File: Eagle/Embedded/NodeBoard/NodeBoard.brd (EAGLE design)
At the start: 121.7 x 96 mm, 68 parts, among them IC1 7812TV, IC2 5v, IC3 3v3, IC4 REG1117, IC5 REG1117, J1 DCJ0202, Q2 IRF740, T1 BC547

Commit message: Minor Eagle Board fixes
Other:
- board size 121.7 x 96 mm -> 121.3 x 95.8 mm

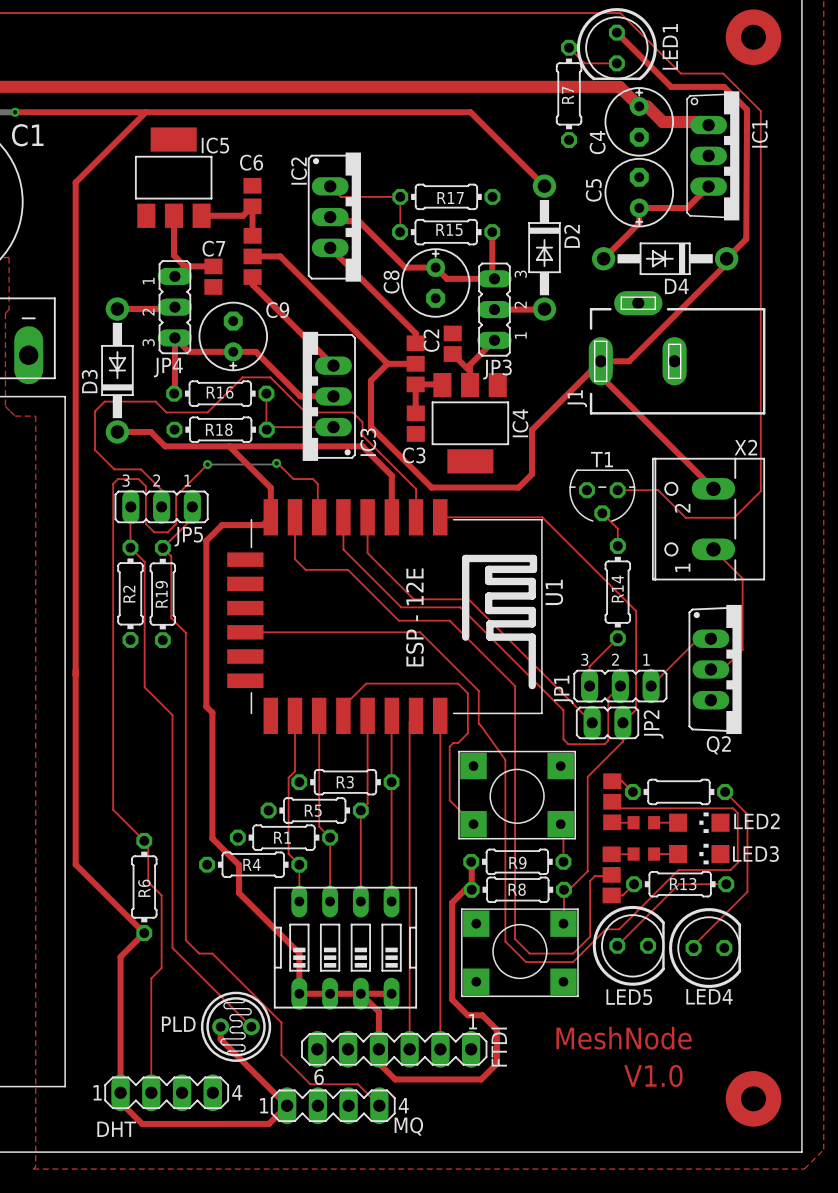
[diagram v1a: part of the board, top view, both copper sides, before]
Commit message: Eagle Flipped directional components
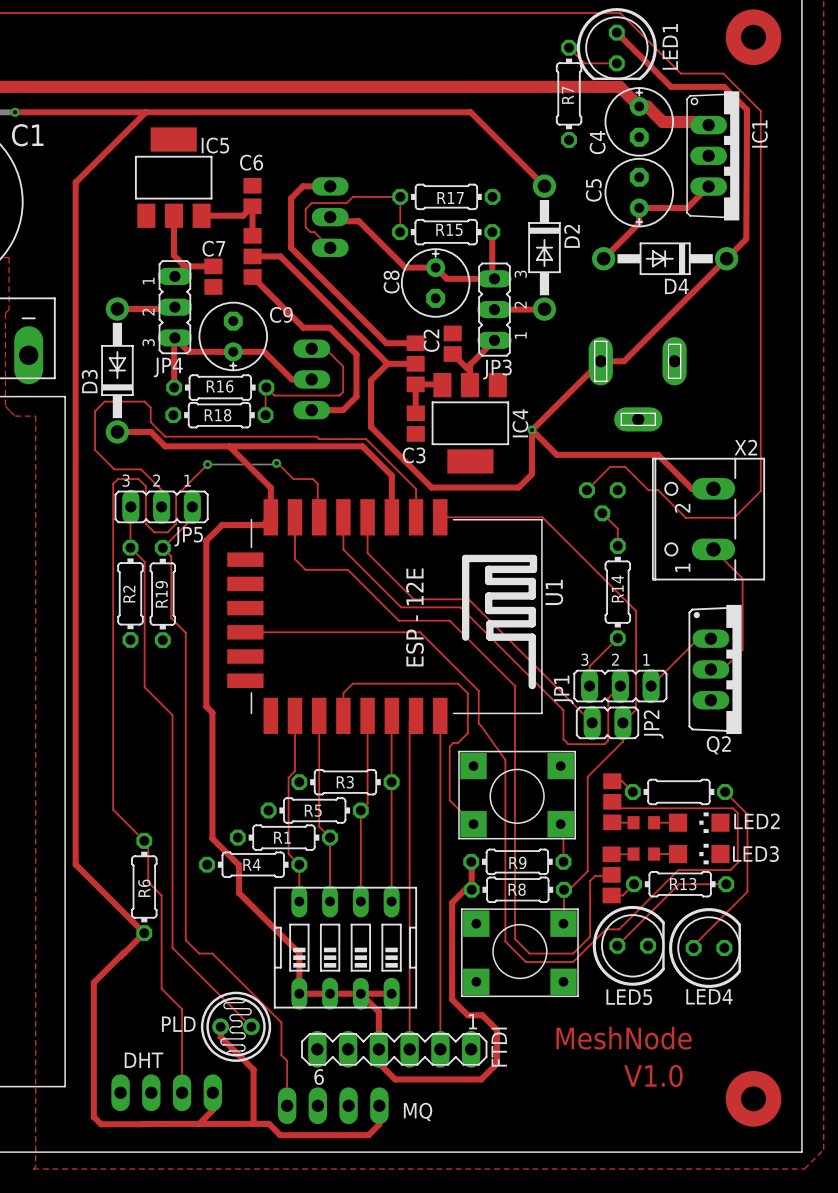
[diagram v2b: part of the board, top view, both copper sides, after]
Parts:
- moved IC3 2.28 mm to (-48.3, 147.6), flipped to the bottom, turned to 270 degrees
- moved R18 1.20 mm to (-53.4, 144.7)
- moved R16 0.50 mm to (-53.4, 147.0)
- flipped DHT to the bottom
- flipped IC2 to the bottom, turned to 90 degrees
- flipped J1 to the bottom, turned to 270 degrees
- flipped MQ to the bottom
- flipped T1 to the bottom
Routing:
- net VCC: track 199.3 -> 215.9 mm
- net N$49: track 10.8 -> 21.3 mm
- net N$50: track 10.1 -> 18.9 mm
- net N$46: track 9.07 -> 15.4 mm
- net N$48: track 8.59 -> 14.4 mm
- net N$9: track 60.8 -> 55.4 mm
- net N$42: track 154.3 -> 158.4 mm
- net N$47: track 19.7 -> 17.3 mm
- net 12V: track 105.4 -> 107.7 mm, vias 0 -> 1
- net N$3: track 46.7 -> 44.4 mm
- net N$22: track 24.7 -> 26.1 mm

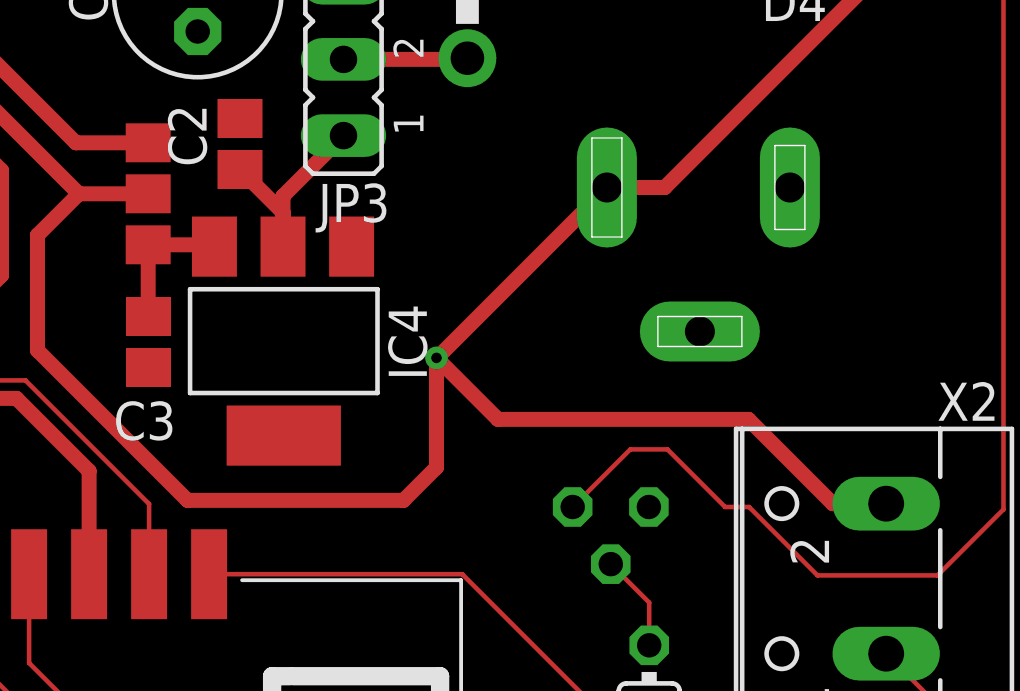
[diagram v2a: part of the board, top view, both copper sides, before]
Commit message: Eagle via fix
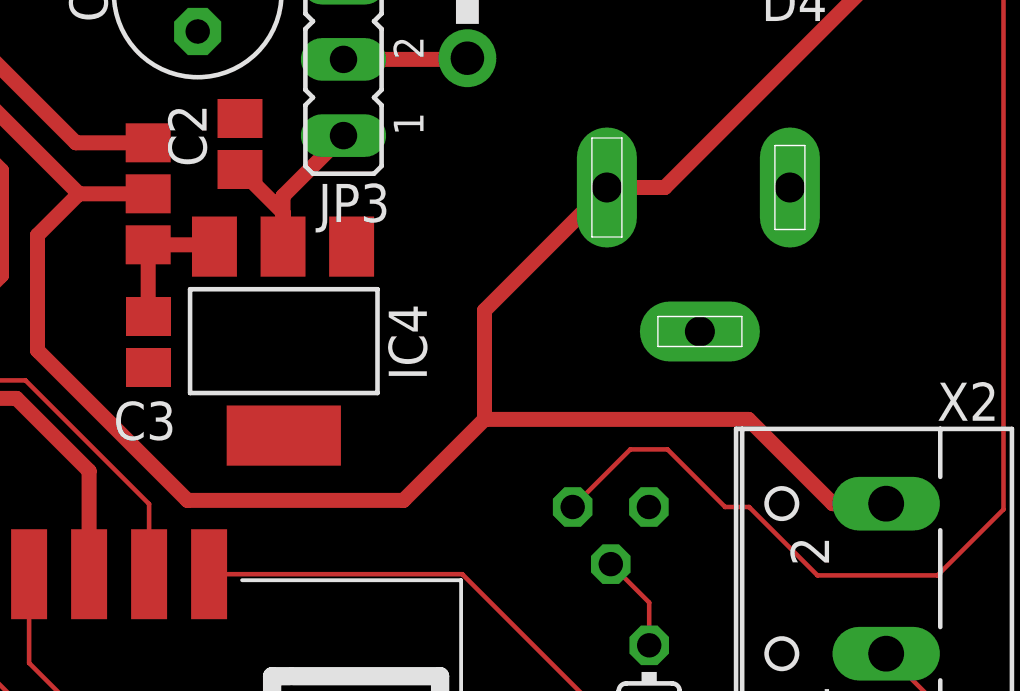
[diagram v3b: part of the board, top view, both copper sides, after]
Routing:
- net 12V: track 107.7 -> 105.3 mm, vias 1 -> 0
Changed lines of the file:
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@@
 <layer number="45" name="Holes" color="7" fill="1" visible="yes" active="yes"/>
 <layer number="46" name="Milling" color="3" fill="1" visible="yes" active="yes"/>
-<layer number="47" name="Measures" color="7" fill="1" visible="yes" active="yes"/>
-<layer number="48" name="Document" color="7" fill="1" visible="yes" active="yes"/>
-<layer number="49" name="Reference" color="7" fill="1" visible="yes" active="yes"/>
+<layer number="47" name="Measures" color="7" fill="1" visible="no" active="yes"/>
+<layer number="48" name="Document" color="7" fill="1" visible="no" active="yes"/>
+<layer number="49" name="Reference" color="7" fill="1" visible="no" active="yes"/>
 <layer number="50" name="dxf" color="7" fill="1" visible="no" active="no"/>
 <layer number="51" name="tDocu" color="7" fill="1" visible="yes" active="yes"/>
@@
 <wire x1="-48.39" y1="157.79" x2="-50.68" y2="157.79" width="0.5" layer="1"/>
 <wire x1="-39.52" y1="148.92" x2="-48.39" y2="157.79" width="0.5" layer="1"/>
-<wire x1="-27.6" y1="139.8" x2="-27.6" y2="143.45" width="0.5" layer="1"/>
-<wire x1="-27.6" y1="139.8" x2="-28.7" y2="138.7" width="0.5" layer="1"/>
 <wire x1="-35.9" y1="138.7" x2="-40.9" y2="143.7" width="0.5" layer="1"/>
 <wire x1="-40.9" y1="143.7" x2="-40.9" y2="147.54" width="0.5" layer="1"/>
 <wire x1="-40.9" y1="147.54" x2="-39.52" y2="148.92" width="0.5" layer="1"/>
-<wire x1="-28.7" y1="138.7" x2="-35.9" y2="138.7" width="0.5" layer="1"/>
-<via x="-27.6" y="143.45" extent="1-16" drill="0.35"/>
+<wire x1="-35.9" y1="138.7" x2="-28.7" y2="138.7" width="0.5" layer="1"/>
 <wire x1="-11.52" y1="157.6" x2="-19.99" y2="149.13" width="0.5" layer="1"/>
 <wire x1="-12.61" y1="138.59" x2="-14.39" y2="138.59" width="0.5" layer="1"/>
-<wire x1="-14.39" y1="138.59" x2="-17.2" y2="141.4" width="0.5" layer="1"/>
-<wire x1="-17.2" y1="141.4" x2="-25.55" y2="141.4" width="0.5" layer="1"/>
-<wire x1="-25.55" y1="141.4" x2="-27.6" y2="143.45" width="0.5" layer="1"/>
+<wire x1="-17.2" y1="141.4" x2="-14.39" y2="138.59" width="0.5" layer="1"/>
 <wire x1="-21.9" y1="149.13" x2="-19.99" y2="149.13" width="0.5" layer="1"/>
 <wire x1="-21.9" y1="149.13" x2="-21.92" y2="149.13" width="0.5" layer="1"/>
-<wire x1="-27.6" y1="143.45" x2="-27.58" y2="143.45" width="0.5" layer="1"/>
-<wire x1="-27.58" y1="143.45" x2="-21.9" y2="149.13" width="0.5" layer="1"/>
+<wire x1="-28.7" y1="138.7" x2="-26" y2="141.4" width="0.5" layer="1"/>
+<wire x1="-26" y1="141.4" x2="-17.2" y2="141.4" width="0.5" layer="1"/>
+<wire x1="-26" y1="141.4" x2="-26" y2="145.03" width="0.5" layer="1"/>
+<wire x1="-26" y1="145.03" x2="-21.9" y2="149.13" width="0.5" layer="1"/>
 </signal>
 <signal name="N$21">

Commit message: Fix dimentions
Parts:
- moved J1 3.01 mm to (-15.8, 149.3)
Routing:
- net 12V: track 105.3 -> 104.1 mm
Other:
- board size 121.3 x 95.8 mm -> 121.1 x 96 mm
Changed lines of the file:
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@@
 <board>
 <plain>
-<wire x1="-126.6" y1="179.6" x2="-126.6" y2="83.8" width="0" layer="20"/>
-<wire x1="-126.6" y1="83.8" x2="-5.3" y2="83.8" width="0" layer="20"/>
-<wire x1="-5.3" y1="83.8" x2="-5.3" y2="179.6" width="0" layer="20"/>
-<wire x1="-5.3" y1="179.6" x2="-126.6" y2="179.6" width="0" layer="20"/>
+<wire x1="-126.4" y1="179.7" x2="-126.3" y2="83.7" width="0" layer="20"/>
+<wire x1="-126.3" y1="83.7" x2="-5.3" y2="83.7" width="0" layer="20"/>
+<wire x1="-5.3" y1="83.7" x2="-5.3" y2="179.7" width="0" layer="20"/>
+<wire x1="-5.3" y1="179.7" x2="-126.4" y2="179.7" width="0" layer="20"/>
 <circle x="-120.5" y="89.7" radius="1.66433125" width="1.27" layer="1"/>
 <circle x="-121.4" y="176" radius="1.66433125" width="1.27" layer="1"/>
@@
 <text x="-25.8" y="92.3" size="1.778" layer="1">MeshNode</text>
 <text x="-20" y="89.2" size="1.778" layer="1">V1.0</text>
+<dimension x1="-126.3" y1="179.6" x2="-5.3" y2="179.6" x3="-65.8" y3="183.3" textsize="1.778" layer="1"/>
+<dimension x1="-126.3" y1="179.7" x2="-126.3" y2="83.7" x3="-127.8" y3="131.7" textsize="1.778" layer="1"/>
 </plain>
 <attributes>
@@
 <attribute name="OC_NEWARK" value="14P6981" x="-57.2" y="164.3" size="1.778" layer="27" display="off"/>
 </element>
-<element name="J1" library="con-jack" package="DCJ0202" value="DCJ0202" x="-18.82" y="149.13" smashed="yes" rot="MR270">
-<attribute name="MF" value="" x="-18.82" y="149.13" size="1.778" layer="28" rot="MR270" display="off"/>
-<attribute name="MPN" value="" x="-18.82" y="149.13" size="1.778" layer="28" rot="MR270" display="off"/>
-<attribute name="NAME" x="-23.4" y="152.84" size="1.27" layer="26" rot="MR270"/>
-<attribute name="OC_FARNELL" value="unknown" x="-18.82" y="149.13" size="1.778" layer="28" rot="MR270" display="off"/>
-<attribute name="OC_NEWARK" value="unknown" x="-18.82" y="149.13" size="1.778" layer="28" rot="MR270" display="off"/>
+<element name="J1" library="con-jack" package="DCJ0202" value="DCJ0202" x="-15.82" y="149.33" smashed="yes" rot="MR270">
+<attribute name="MF" value="" x="-15.82" y="149.33" size="1.778" layer="28" rot="MR270" display="off"/>
+<attribute name="MPN" value="" x="-15.82" y="149.33" size="1.778" layer="28" rot="MR270" display="off"/>
+<attribute name="NAME" x="-20.4" y="153.04" size="1.27" layer="26" rot="MR270"/>
+<attribute name="OC_FARNELL" value="unknown" x="-15.82" y="149.33" size="1.778" layer="28" rot="MR270" display="off"/>
+<attribute name="OC_NEWARK" value="unknown" x="-15.82" y="149.33" size="1.778" layer="28" rot="MR270" display="off"/>
 </element>
 <element name="JMP3" library="jump-0r-smd" package="A0R-JMP" value="0R-JUMPA" x="-20.97" y="112.74" smashed="yes"/>
@@
 <wire x1="-40.9" y1="147.54" x2="-39.52" y2="148.92" width="0.5" layer="1"/>
 <wire x1="-35.9" y1="138.7" x2="-28.7" y2="138.7" width="0.5" layer="1"/>
-<wire x1="-11.52" y1="157.6" x2="-19.99" y2="149.13" width="0.5" layer="1"/>
 <wire x1="-12.61" y1="138.59" x2="-14.39" y2="138.59" width="0.5" layer="1"/>
 <wire x1="-17.2" y1="141.4" x2="-14.39" y2="138.59" width="0.5" layer="1"/>
-<wire x1="-21.9" y1="149.13" x2="-19.99" y2="149.13" width="0.5" layer="1"/>
-<wire x1="-21.9" y1="149.13" x2="-21.92" y2="149.13" width="0.5" layer="1"/>
 <wire x1="-28.7" y1="138.7" x2="-26" y2="141.4" width="0.5" layer="1"/>
 <wire x1="-26" y1="141.4" x2="-17.2" y2="141.4" width="0.5" layer="1"/>
-<wire x1="-26" y1="141.4" x2="-26" y2="145.03" width="0.5" layer="1"/>
-<wire x1="-26" y1="145.03" x2="-21.9" y2="149.13" width="0.5" layer="1"/>
+<wire x1="-26" y1="141.4" x2="-26" y2="142.25" width="0.5" layer="1"/>
+<wire x1="-26" y1="142.25" x2="-18.92" y2="149.33" width="0.5" layer="1"/>
+<wire x1="-18.92" y1="149.33" x2="-11.52" y2="156.73" width="0.5" layer="1"/>
+<wire x1="-11.52" y1="156.73" x2="-11.52" y2="157.6" width="0.5" layer="1"/>
 </signal>
 <signal name="N$21">

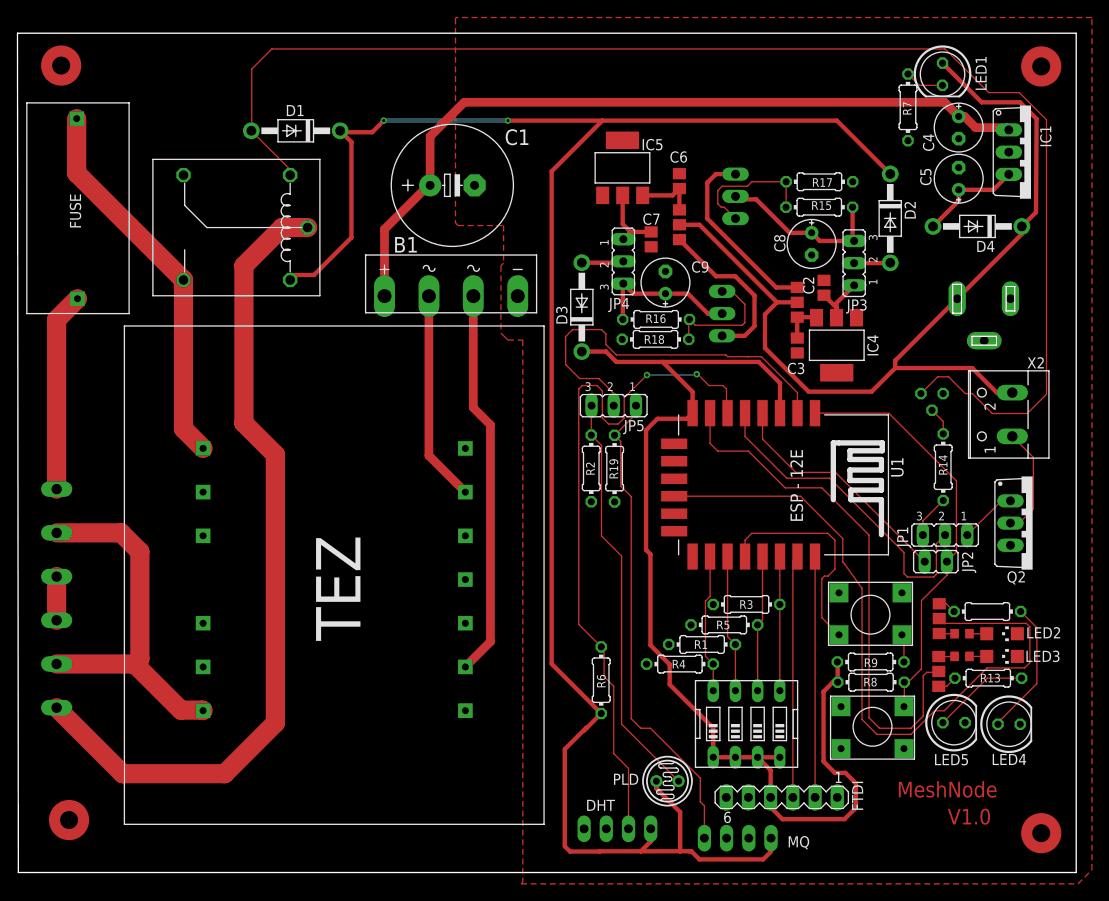
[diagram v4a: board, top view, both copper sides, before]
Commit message: Eagle 121x96 end dimention
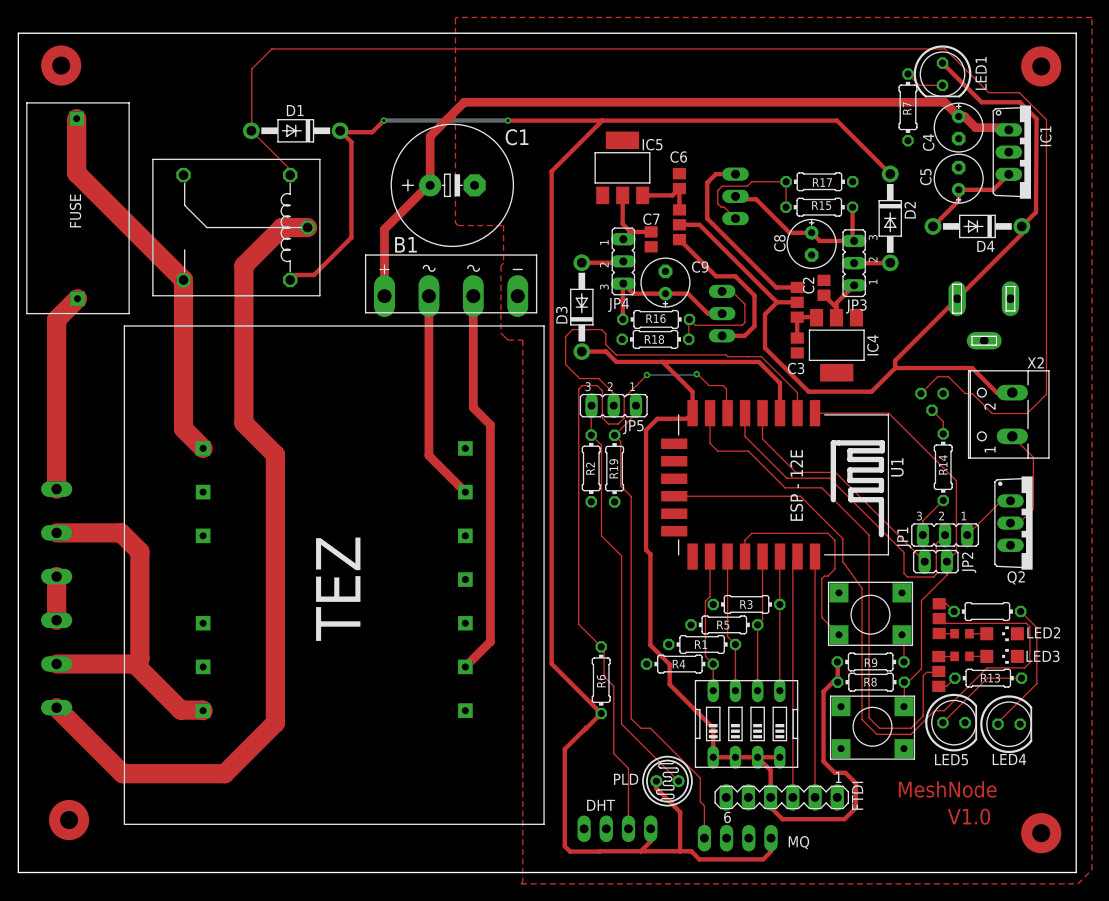
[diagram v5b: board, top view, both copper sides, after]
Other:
- board size 121.1 x 96 mm -> 121 x 96 mm

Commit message: Eagle pcb v2.0
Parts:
- moved C8 14.6 mm to (-41.1, 169.1), turned to 90 degrees
- moved C7 11.8 mm to (-60.8, 165.7), turned to 180 degrees
- moved JMP5 9.10 mm to (-40.7, 157.3)
- moved IC5 8.92 mm to (-59.9, 172.8)
- moved C6 8.69 mm to (-52.5, 171.3)
- moved R7 8.46 mm to (-29.7, 177.9), turned to 0 degrees
- moved C3 7.93 mm to (-42.5, 149.9)
- moved JMP8 7.89 mm to (-52.4, 165.5)
- moved IC3 7.69 mm to (-49.5, 155.2)
- moved IC2 7.25 mm to (-44.7, 167.6)
- moved D3 7.16 mm to (-63.4, 155.4)
- moved C4 6.96 mm to (-20.6, 162.2), turned to 90 degrees
- moved C2 6.56 mm to (-35.0, 157.1)
- moved C5 6.47 mm to (-20.7, 169.2), turned to 270 degrees
- moved T1 6.25 mm to (-26.2, 142.9), turned to 270 degrees
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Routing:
- net N$35: track 80.9 -> 39.2 mm
- net N$53: track 11.9 -> 34.7 mm
- net 19V: track 89.7 -> 106.2 mm
- net 3V3: track 126.3 -> 141.4 mm, vias 0 -> 2
- net N$3: track 44.4 -> 31.6 mm, vias 0 -> 1
- net 12V: track 104.1 -> 114.2 mm, vias 0 -> 1
- net N$56: track 4.63 -> 13.2 mm
- net N$41: track 3.24 -> 11.5 mm
- net N$29: track 48.2 -> 56.0 mm, vias 0 -> 1
- net N$38: track 60.7 -> 67.4 mm, vias 0 -> 2
- net N$21: track 27.4 -> 33.9 mm, vias 0 -> 1
- net N$9: track 55.4 -> 61.2 mm
- net N$45: track 19.6 -> 24.9 mm
- net N$42: track 158.4 -> 163.4 mm, vias 0 -> 2
- net N$48: track 14.4 -> 19.1 mm
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- added copper zone on layer 16, net GND
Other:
- board text added: "V2.0"
- board text removed: "V1.0"
